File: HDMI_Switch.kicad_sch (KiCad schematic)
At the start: 16 parts, among them U11 HD3SS215RTQR

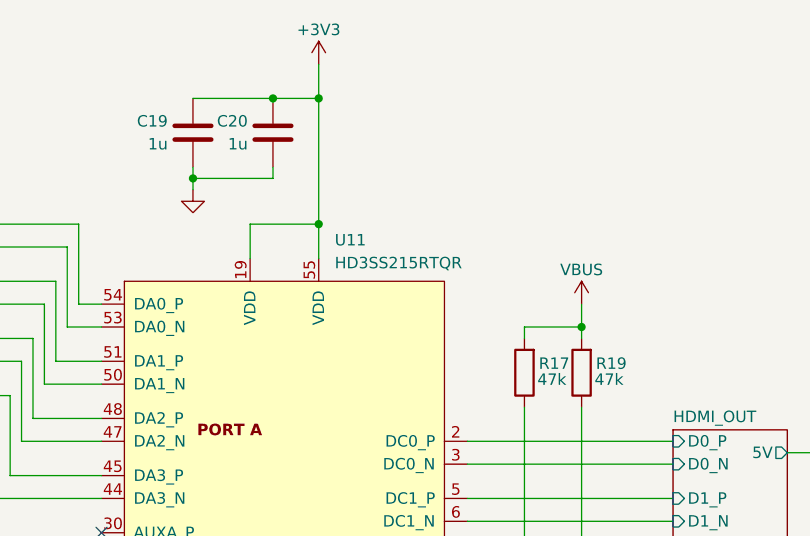
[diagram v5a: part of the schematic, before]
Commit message: Updated library structure
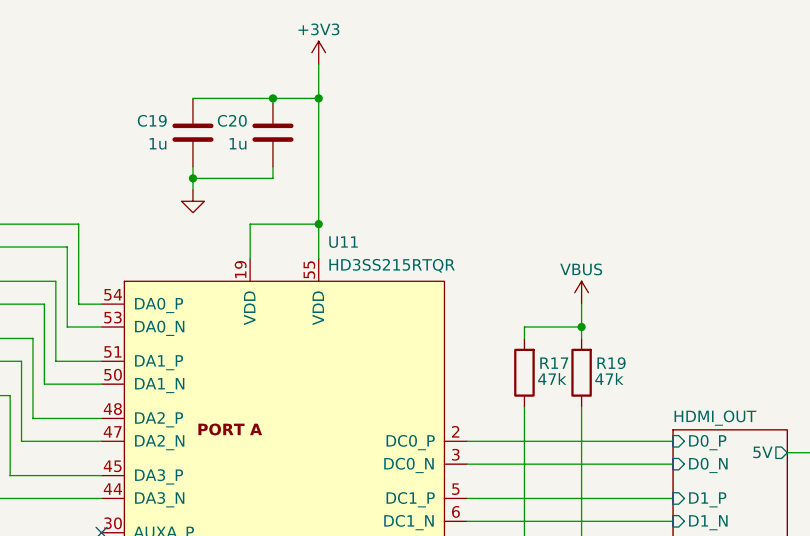
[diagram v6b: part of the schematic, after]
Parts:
- removed U11: HD3SS215RTQR, Package_DFN_QFN:QFN-56-1EP_8x8mm_P0.5mm_EP4.3x4.3mm, symbol HD3SS215RTQR:HD3SS215RTQR
- added U11: HD3SS215RTQR, Package_DFN_QFN:QFN-56-1EP_8x8mm_P0.5mm_EP4.3x4.3mm, symbol Symbols:HD3SS215RTQR
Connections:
- net +3V3: now also U11.19 (VDD), U11.43 (OE), U11.55 (VDD)
- net GND: now also U11.10 (GND), U11.33 (GND), U11.36 (GND), U11.39 (GND), U11.4 (GND), U11.46 (GND), U11.49 (GND), U11.52 (GND), U11.57 (GND), U11.7 (GND)
- net HDMI_IN_A/CK_N: now also U11.44 (DA3_N)
- net HDMI_IN_A/CK_P: now also U11.45 (DA3_P)
- net HDMI_IN_A/D0_N: now also U11.53 (DA0_N)
- net HDMI_IN_A/D0_P: now also U11.54 (DA0_P)
- net HDMI_IN_A/D1_N: now also U11.50 (DA1_N)
- net HDMI_IN_A/D1_P: now also U11.51 (DA1_P)
- net HDMI_IN_A/D2_N: now also U11.47 (DA2_N)
- net HDMI_IN_A/D2_P: now also U11.48 (DA2_P)
- net HDMI_IN_A/HPD: now also U11.16 (HPDA)
- net HDMI_IN_A/SCL: now also U11.27 (DDCCLK_A)
- net HDMI_IN_A/SDA: now also U11.28 (DDCDAT_A)
- net HDMI_IN_B/CK_N: now also U11.31 (DB3_N)
- net HDMI_IN_B/CK_P: now also U11.32 (DB3_P)
- net HDMI_IN_B/D0_N: now also U11.40 (DB0_N)
- net HDMI_IN_B/D0_P: now also U11.41 (DB0_P)
- net HDMI_IN_B/D1_N: now also U11.37 (DB1_N)
- net HDMI_IN_B/D1_P: now also U11.38 (DB1_P)
- net HDMI_IN_B/D2_N: now also U11.34 (DB2_N)
- net HDMI_IN_B/D2_P: now also U11.35 (DB2_P)
- net HDMI_IN_B/HPD: now also U11.17 (HPDB)
- net HDMI_IN_B/SCL: now also U11.22 (DDCCLK_B)
- net HDMI_IN_B/SDA: now also U11.23 (DDCDAT_B)
- net HDMI_OUT/CK_N: now also U11.12 (DC3_N)
- net HDMI_OUT/CK_P: now also U11.11 (DC3_P)
- net HDMI_OUT/D0_N: now also U11.3 (DC0_N)
- net HDMI_OUT/D0_P: now also U11.2 (DC0_P)
- net HDMI_OUT/D1_N: now also U11.6 (DC1_N)
- net HDMI_OUT/D1_P: now also U11.5 (DC1_P)
- net HDMI_OUT/D2_N: now also U11.9 (DC2_N)
- net HDMI_OUT/D2_P: now also U11.8 (DC2_P)
- net HDMI_OUT/HPD: now also U11.15 (HPDC)
- net HDMI_OUT/SCL: now also U11.18 (DDCCLK_C)
- net HDMI_OUT/SDA: now also U11.26 (DDCDAT_C)
- net SW: now also U11.56 (Dx_SEL)
- net at R20.2, R21.1: now also U11.1 (AUX_SEL)
- new net: U11.20 (NC), U11.21 (NC), U11.42 (NC)
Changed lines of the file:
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@@
 	)
 	(junction
-		(at 199.39 72.39)
-		(diameter 0)
-		(color 0 0 0 0)
-	)
-	(junction
 		(at 71.12 48.26)
 		(diameter 0)
@@
 	)
 	(junction
+		(at 199.39 72.39)
+		(diameter 0)
+		(color 0 0 0 0)
+	)
+	(junction
 		(at 165.1 102.87)
 		(diameter 0)
@@
 	)
 	(symbol
-		(lib_id "HD3SS215RTQR:HD3SS215RTQR")
-		(at 138.43 95.25 0)
-		(unit 1)
-		(body_style 1)
-		(exclude_from_sim no)
-		(in_bom yes)
-		(on_board yes)
-		(in_pos_files yes)
-		(dnp no)
-		(property "Reference" "U11"
-			(at 144.018 48.768 0)
-			(show_name no)
-			(do_not_autoplace no)
-			(effects
-				(font
-					(size 1.27 1.27)
-				)
-				(justify left)
-			)
-		)
-		(property "Value" "HD3SS215RTQR"
-			(at 144.018 51.308 0)
-			(show_name no)
-			(do_not_autoplace no)
-			(effects
-				(font
-					(size 1.27 1.27)
-				)
-				(justify left)
-			)
-		)
-		(property "Footprint" "Package_DFN_QFN:QFN-56-1EP_8x8mm_P0.5mm_EP4.3x4.3mm"
-			(at 138.43 95.25 0)
-			(hide yes)
-			(show_name no)
-			(do_not_autoplace no)
-			(effects
-				(font
-					(size 1.27 1.27)
-				)
-			)
-		)
-		(property "Datasheet" "https://www.ti.com/lit/ds/symlink/hd3ss215.pdf"
-			(at 138.43 95.25 0)
-			(hide yes)
-			(show_name no)
-			(do_not_autoplace no)
-			(effects
-				(font
-					(size 1.27 1.27)
-				)
-			)
-		)
-		(property "Description" "6-Gbps HDMI / DisplayPort 2:1 / 1:2 differential switch, 56-pin RTQ VQFN"
-			(at 138.43 95.25 0)
-			(hide yes)
-			(show_name no)
-			(do_not_autoplace no)
-			(effects
-				(font
-					(size 1.27 1.27)
-				)
-			)
-		)
-		(property "DigiKey" "296-42335-1-ND"
-			(at 138.43 95.25 0)
-			(hide yes)
-			(show_name no)
-			(do_not_autoplace no)
-			(effects
-				(font
-					(size 1.27 1.27)
-				)
-			)
-		)
-		(pin "13"
-		)
-		(pin "14"
-		)
-		(pin "16"
-		)
-		(pin "15"
-		)
-		(pin "17"
-		)
-		(pin "18"
-		)
-		(pin "12"
-		)
-		(pin "11"
-		)
-		(pin "10"
-		)
-		(pin "9"
-		)
-		(pin "8"
-		)
-		(pin "7"
-		)
-		(pin "5"
-		)
-		(pin "1"
-		)
-		(pin "19"
-		)
-		(pin "20"
-		)
-		(pin "2"
-		)
-		(pin "3"
-		)
-		(pin "4"
-		)
-		(pin "6"
-		)
-		(pin "41"
-		)
-		(pin "42"
-		)
-		(pin "43"
-		)
-		(pin "46"
-		)
-		(pin "44"
-		)
-		(pin "45"
-		)
-		(pin "39"
-		)
-		(pin "40"
-		)
-		(pin "38"
-		)
-		(pin "37"
-		)
-		(pin "36"
-		)
-		(pin "35"
-		)
-		(pin "34"
-		)
-		(pin "33"
-		)
-		(pin "32"
-		)
-		(pin "31"
-		)
-		(pin "30"
-		)
-		(pin "29"
-		)
-		(pin "28"
-		)
-		(pin "27"
-		)
-		(pin "55"
-		)
-		(pin "50"
-		)
-		(pin "49"
-		)
-		(pin "48"
-		)
-		(pin "47"
-		)
-		(pin "57"
-		)
-		(pin "54"
-		)
-		(pin "53"
-		)
-		(pin "56"
-		)
-		(pin "52"
-		)
-		(pin "51"
-		)
-		(pin "21"
-		)
-		(pin "22"
-		)
-		(pin "23"
-		)
-		(pin "24"
-		)
-		(pin "25"
-		)
-		(pin "26"
-		)
-		(instances
-			(project "KVM_Switch"
-				(path "/94386106-ccd4-487f-b5c5-d52ec3dd59db/6e43926c-16e0-4a92-a7fc-ce5a89c8ce59"
-					(reference "U11")
-					(unit 1)
-				)
-			)
-		)
-	)
-	(symbol
 		(lib_id "Connector:TestPoint")
 		(at 88.9 72.39 270)
@@
 					(unit 1)
 				)
+			)
+		)
+	)
+	(symbol
+		(lib_id "Symbols:HD3SS215RTQR")
+		(at 138.43 95.25 0)
+		(unit 1)
+		(body_style 1)
+		(exclude_from_sim no)
+		(in_bom yes)
+		(on_board yes)
+		(in_pos_files yes)
+		(dnp no)
+		(property "Reference" "U11"
+			(at 143.256 49.022 0)
+			(show_name no)
+			(do_not_autoplace no)
+			(effects
+				(font
+					(size 1.27 1.27)
+				)
+				(justify left)
+			)
+		)
+		(property "Value" "HD3SS215RTQR"
+			(at 143.256 51.562 0)
+			(show_name no)
+			(do_not_autoplace no)
+			(effects
+				(font
+					(size 1.27 1.27)
+				)
+				(justify left)
+			)
+		)
+		(property "Footprint" "Package_DFN_QFN:QFN-56-1EP_8x8mm_P0.5mm_EP4.3x4.3mm"
+			(at 138.43 100.838 0)
+			(hide yes)
+			(show_name no)
+			(do_not_autoplace no)
+			(effects
+				(font
+					(size 1.27 1.27)
+				)
+			)
+		)
+		(property "Datasheet" "https://www.ti.com/lit/ds/symlink/hd3ss215.pdf"
+			(at 138.43 97.536 0)
+			(hide yes)
+			(show_name no)
+			(do_not_autoplace no)
+			(effects
+				(font
+					(size 1.27 1.27)
+				)
+			)
+		)
+		(property "Description" "6-Gbps HDMI / DisplayPort 2:1 / 1:2 differential switch, 56-pin RTQ VQFN"
+			(at 138.43 103.886 0)
+			(hide yes)
+			(show_name no)
+			(do_not_autoplace no)
+			(effects
+				(font
+					(size 1.27 1.27)
+				)
+			)
+		)
+		(property "DigiKey" "296-42335-1-ND"
+			(at 138.43 95.25 0)
+			(hide yes)
+			(show_name no)
+			(do_not_autoplace no)
+			(effects
+				(font
+					(size 1.27 1.27)
+				)
+			)
+		)
+		(pin "53"
+		)
+		(pin "57"
+		)
+		(pin "56"
+		)
+		(pin "55"
+		)
+		(pin "54"
+		)
+		(pin "52"
+		)
+		(pin "51"
+		)
+		(pin "50"
+		)
+		(pin "49"
+		)
+		(pin "48"
+		)
+		(pin "47"
+		)
+		(pin "46"
+		)
+		(pin "45"
+		)
+		(pin "44"
+		)
+		(pin "43"
+		)
+		(pin "22"
+		)
+		(pin "21"
+		)
+		(pin "13"
+		)
+		(pin "36"
+		)
+		(pin "39"
+		)
+		(pin "35"
+		)
+		(pin "37"
+		)
+		(pin "38"
+		)
+		(pin "40"
+		)
+		(pin "12"
+		)
+		(pin "19"
+		)
+		(pin "17"
+		)
+		(pin "16"
+		)
+		(pin "18"
+		)
+		(pin "20"
+		)
+		(pin "1"
+		)
+		(pin "2"
+		)
+		(pin "7"
+		)
+		(pin "9"
+		)
+		(pin "5"
+		)
+		(pin "4"
+		)
+		(pin "11"
+		)
+		(pin "6"
+		)
+		(pin "8"
+		)
+		(pin "3"
+		)
+		(pin "10"
+		)
+		(pin "15"
+		)
+		(pin "42"
+		)
+		(pin "41"
+		)
+		(pin "28"
+		)
+		(pin "27"
+		)
+		(pin "30"
+		)
+		(pin "29"
+		)
+		(pin "32"
+		)
+		(pin "33"
+		)
+		(pin "31"
+		)
+		(pin "34"
+		)
+		(pin "25"
+		)
+		(pin "23"
+		)
+		(pin "26"
+		)
+		(pin "24"
+		)
+		(pin "14"
+		)
+		(instances
+			(project "KVM_Switch"
+				(path "/94386106-ccd4-487f-b5c5-d52ec3dd59db/6e43926c-16e0-4a92-a7fc-ce5a89c8ce59"
+					(reference "U11")
+					(unit 1)
+				)

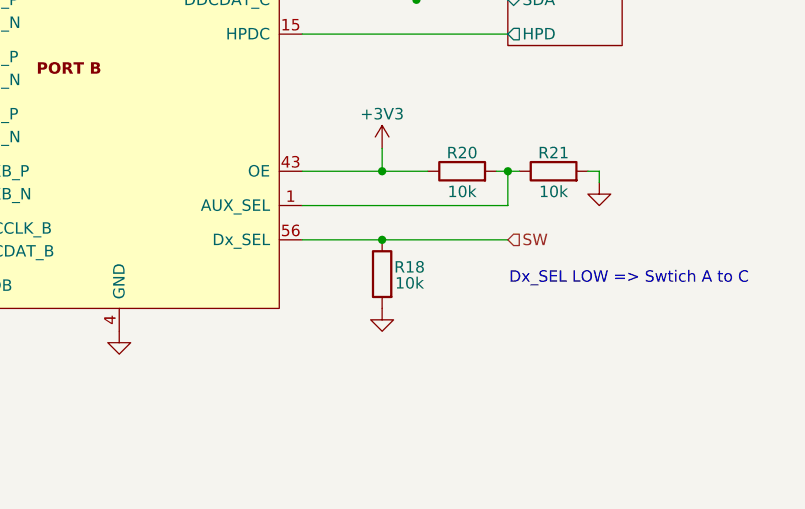
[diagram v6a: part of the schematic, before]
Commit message: Library and Schematics Fixes
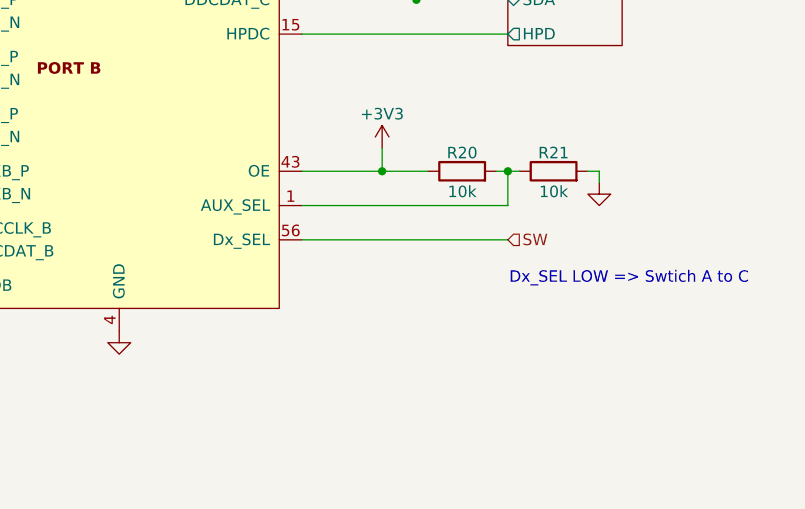
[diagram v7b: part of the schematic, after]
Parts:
- removed R18: 10k, Resistor_SMD:R_0402_1005Metric, symbol Device:R
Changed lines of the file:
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@@
-	)
-	(junction
-		(at 167.64 132.08)
-		(diameter 0)
-		(color 0 0 0 0)
 	)
 	(junction
@@
 	(wire
 		(pts
-			(xy 167.64 132.08) (xy 181.61 132.08)
+			(xy 158.75 132.08) (xy 181.61 132.08)
 		)
 		(stroke
@@
 		(pts
 			(xy 165.1 58.42) (xy 171.45 58.42)
-		)
-		(stroke
-			(width 0)
-			(type default)
-		)
-	)
-	(wire
-		(pts
-			(xy 158.75 132.08) (xy 167.64 132.08)
 		)
 		(stroke
@@
 	)
 	(symbol
-		(lib_id "Device:R")
-		(at 167.64 135.89 0)
-		(mirror y)
-		(unit 1)
-		(body_style 1)
-		(exclude_from_sim no)
-		(in_bom yes)
-		(on_board yes)
-		(in_pos_files yes)
-		(dnp no)
-		(property "Reference" "R18"
-			(at 170.688 135.128 0)
-			(show_name no)
-			(do_not_autoplace no)
-			(effects
-				(font
-					(size 1.27 1.27)
-				)
-			)
-		)
-		(property "Value" "10k"
-			(at 170.688 136.906 0)
-			(show_name no)
-			(do_not_autoplace no)
-			(effects
-				(font
-					(size 1.27 1.27)
-				)
-			)
-		)
-		(property "Footprint" "Resistor_SMD:R_0402_1005Metric"
-			(at 169.418 135.89 90)
-			(hide yes)
-			(show_name no)
-			(do_not_autoplace no)
-			(effects
-				(font
-					(size 1.27 1.27)
-				)
-			)
-		)
-		(property "Datasheet" ""
-			(at 167.64 135.89 0)
-			(hide yes)
-			(show_name no)
-			(do_not_autoplace no)
-			(effects
-				(font
-					(size 1.27 1.27)
-				)
-			)
-		)
-		(property "Description" "Resistor"
-			(at 167.64 135.89 0)
-			(hide yes)
-			(show_name no)
-			(do_not_autoplace no)
-			(effects
-				(font
-					(size 1.27 1.27)
-				)
-			)
-		)
-		(property "AX" "201002"
-			(at 167.64 135.89 0)
-			(hide yes)
-			(show_name no)
-			(do_not_autoplace no)
-			(effects
-				(font
-					(size 1.27 1.27)
-				)
-			)
-		)
-		(pin "2"
-		)
-		(pin "1"
-		)
-		(instances
-			(project "KVM_Switch"
-				(path "/94386106-ccd4-487f-b5c5-d52ec3dd59db/6e43926c-16e0-4a92-a7fc-ce5a89c8ce59"
-					(reference "R18")
-					(unit 1)
-				)
-			)
-		)
-	)
-	(symbol
 		(lib_id "power:GND")
 		(at 191.77 125.73 0)
@@
 					(unit 1)
 				)
-			)
-		)
-	)
-	(symbol
-		(lib_id "power:GND")
-		(at 167.64 139.7 0)
-		(unit 1)
-		(body_style 1)
-		(exclude_from_sim no)
-		(in_bom yes)
-		(on_board yes)
-		(in_pos_files yes)
-		(dnp no)
-		(property "Reference" "#PWR029"
-			(at 167.64 146.05 0)
-			(hide yes)
-			(show_name no)
-			(do_not_autoplace no)
-			(effects
-				(font
-					(size 1.27 1.27)
-				)
-			)
-		)
-		(property "Value" "GND"
-			(at 167.64 143.51 0)
-			(hide yes)
-			(show_name no)
-			(do_not_autoplace no)
-			(effects
-				(font
-					(size 1.27 1.27)
-				)
-			)
-		)
-		(property "Footprint" ""
-			(at 167.64 139.7 0)
-			(hide yes)
-			(show_name no)
-			(do_not_autoplace no)
-			(effects
-				(font
-					(size 1.27 1.27)
-				)
-			)
-		)
-		(property "Datasheet" ""
-			(at 167.64 139.7 0)
-			(hide yes)
-			(show_name no)
-			(do_not_autoplace no)
-			(effects
-				(font
-					(size 1.27 1.27)
-				)
-			)
-		)
-		(property "Description" "Power symbol creates a global label with name \"GND\" , ground"
-			(at 167.64 139.7 0)
-			(hide yes)
-			(show_name no)
-			(do_not_autoplace no)
-			(effects
-				(font
-					(size 1.27 1.27)
-				)
-			)
-		)
-		(pin "1"
-		)
-		(instances
-			(project "KVM_Switch"
-				(path "/94386106-ccd4-487f-b5c5-d52ec3dd59db/6e43926c-16e0-4a92-a7fc-ce5a89c8ce59"
-					(reference "#PWR029")
-					(unit 1)
-				)

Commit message: More schematics fixes & Layout attempt
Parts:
- added R8: 10k, Resistor_SMD:R_0402_1005Metric, symbol Device:R
- R5: renamed from R15; footprint Resistor_SMD:R_0603_1608Metric -> Resistor_SMD:R_0402_1005Metric; AX 141003 -> 201003
- R9: renamed from R16; footprint Resistor_SMD:R_0603_1608Metric -> Resistor_SMD:R_0402_1005Metric; AX 141003 -> 201003
- U5: renamed from U11; symbol Symbols:HD3SS215RTQR -> KVM_Swtich:HD3SS215RTQR
- renumbered C19 to C1, C20 to C2, C21 to C3, R17 to R3, R19 to R4, R20 to R6, R21 to R7, TP3 to TP2, TP5 to TP3, TP2 to TP4, TP4 to TP5
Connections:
- net GND: now also R8.2
- net HDMI_IN_A/D0_N: now also U5.47 (DA2_N); no longer U5.53 (DA0_N)
- net HDMI_IN_A/D0_P: now also U5.48 (DA2_P); no longer U5.54 (DA0_P)
- net HDMI_IN_A/D2_N: now also U5.53 (DA0_N); no longer U5.47 (DA2_N)
- net HDMI_IN_A/D2_P: now also U5.54 (DA0_P); no longer U5.48 (DA2_P)
- net HDMI_IN_B/D0_N: now also U5.34 (DB2_N); no longer U5.40 (DB0_N)
- net HDMI_IN_B/D0_P: now also U5.35 (DB2_P); no longer U5.41 (DB0_P)
- net HDMI_IN_B/D2_N: now also U5.40 (DB0_N); no longer U5.34 (DB2_N)
- net HDMI_IN_B/D2_P: now also U5.41 (DB0_P); no longer U5.35 (DB2_P)
- net HDMI_OUT/D0_N: now also U5.9 (DC2_N); no longer U5.3 (DC0_N)
- net HDMI_OUT/D0_P: now also U5.8 (DC2_P); no longer U5.2 (DC0_P)
- net HDMI_OUT/D2_N: now also U5.3 (DC0_N); no longer U5.9 (DC2_N)
- net HDMI_OUT/D2_P: now also U5.2 (DC0_P); no longer U5.8 (DC2_P)
- net SW: now also R8.1
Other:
- company: (none) -> Stanisław Basiuk
- title: (none) -> KVM_Switch
